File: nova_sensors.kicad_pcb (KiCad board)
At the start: 2 copper layers, 100 x 100 mm, 83 parts, among them J1 Conn_01x02_Socket, J10 Conn_01x03_Socket, J11 Conn_01x03_Socket, J12 Conn_01x03_Socket, J13 Conn_01x03_Socket, J4 Conn_01x04_Socket, J5 Conn_01x02_Socket, J6 Conn_01x02_Socket, J7 Conn_01x02_Socket, J8 Conn_01x02_Socket, J9 Conn_01x02_Socket, SW1 SW_Push, SW2 SW_DIP_x02, SW3 SW_DIP_x02, U1 AT32F455CET7, U2 MAX3232, U3 MAX13487EESA+T, U4 MAX13487EESA+T, U5 LD1117S33TR, U6 XL1509-ADJ, Y1 8Mhz, Y2 32768hz

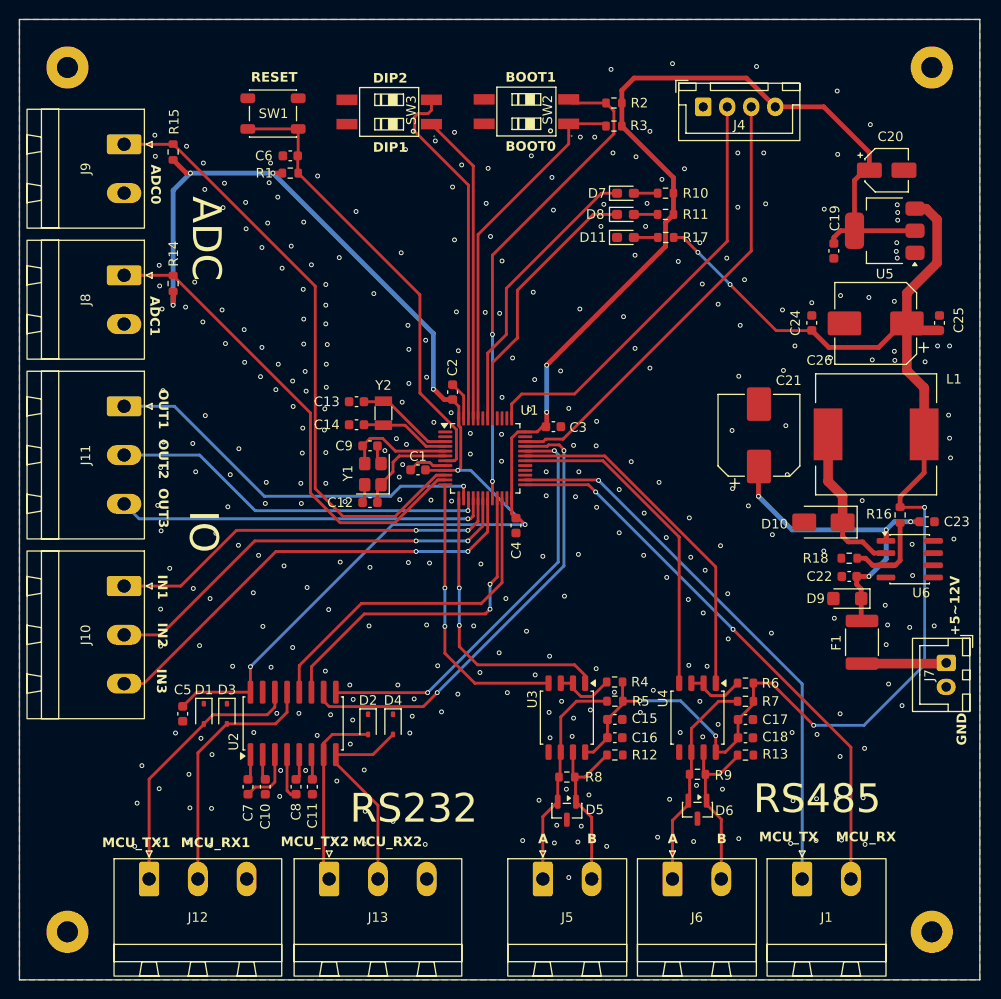
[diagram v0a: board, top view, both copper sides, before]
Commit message: refact: 重新排列引脚，使得布局更合理，同时压缩板子面积
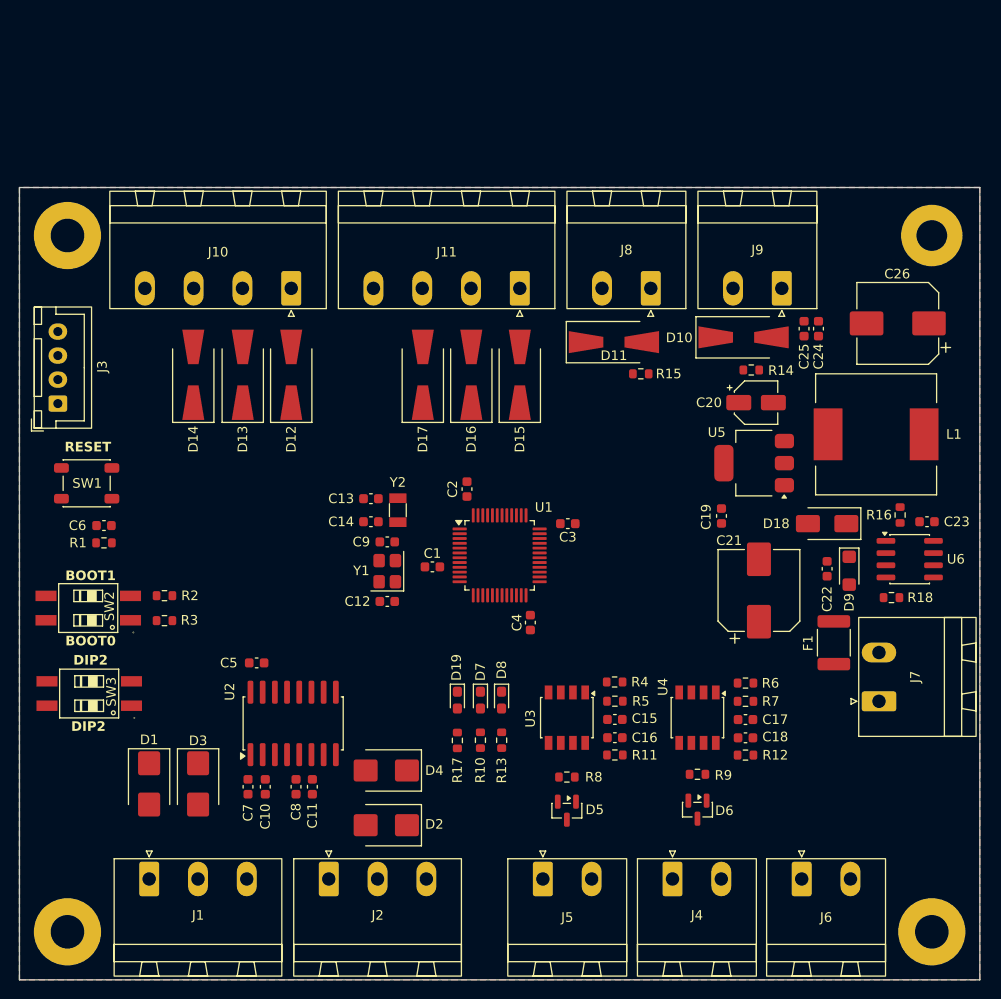
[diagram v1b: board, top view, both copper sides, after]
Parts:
- removed J12, J13: Conn_01x03_Socket, Connector_Phoenix_MSTB:PhoenixContact_MSTBA_2,5_3-G-5,08_1x03_P5.08mm_Horizontal
- added D12: SMAJ3.3CA, Diode_SMD:D_SMA-SMB_Universal_Handsoldering, F.Cu at (28.3, 147.0)
- added D13: SMAJ3.3CA, Diode_SMD:D_SMA-SMB_Universal_Handsoldering, F.Cu at (23.2, 147.0)
- added D14: SMAJ3.3CA, Diode_SMD:D_SMA-SMB_Universal_Handsoldering, F.Cu at (18.1, 147.0)
- added D15: SMAJ3.3CA, Diode_SMD:D_SMA-SMB_Universal_Handsoldering, F.Cu at (52.1, 147.0)
- added D16: SMAJ3.3CA, Diode_SMD:D_SMA-SMB_Universal_Handsoldering, F.Cu at (47.0, 147.0)
- added D17: SMAJ3.3CA, Diode_SMD:D_SMA-SMB_Universal_Handsoldering, F.Cu at (42.0, 147.0)
- added D18: SS34, Diode_SMD:D_SMA, F.Cu at (84.1, 162.5)
- added D19: GREEN, LED_SMD:LED_0603_1608Metric_Pad1.05x0.95mm_HandSolder, F.Cu at (45.6, 180.9)
- added J2: Conn_01x03_Socket, Connector_Phoenix_MSTB:PhoenixContact_MSTBA_2,5_3-G-5,08_1x03_P5.08mm_Horizontal, F.Cu at (32.2, 199.5)
- added J3: Conn_01x04_Socket, Connector_JST:JST_XH_B4B-XH-A_1x04_P2.50mm_Vertical, F.Cu at (4.00, 150.0)
- C24: value 100nF/35V -> 100nF/16V
- C25: value 22uF/35V -> 22uF/16V
- C26: value 220uF/35V -> 220uF/16V
- D1, D2, D3, D4: value SGSD15C -> SMAJ8.0CA; footprint Diode_SMD:D_SOD-323 -> Diode_SMD:D_SMB
- D10: value SS34 -> SMAJ3.3CA; footprint Diode_SMD:D_SMA -> Diode_SMD:D_SMA-SMB_Universal_Handsoldering
- D11: value GREEN -> SMAJ3.3CA; footprint LED_SMD:LED_0603_1608Metric_Pad1.05x0.95mm_HandSolder -> Diode_SMD:D_SMA-SMB_Universal_Handsoldering
- H1: footprint MountingHole:MountingHole_2.2mm_M2_Pad -> MountingHole:MountingHole_3.2mm_M3_Pad
- H2, H3, H4: footprint MountingHole:MountingHole_2.2mm_M2_Pad -> MountingHole:MountingHole_3.5mm_Pad
- J1: value Conn_01x02_Socket -> Conn_01x03_Socket; footprint Connector_Phoenix_MSTB:PhoenixContact_MSTBA_2,5_2-G-5,08_1x02_P5.08mm_Horizontal -> Connector_Phoenix_MSTB:PhoenixContact_MSTBA_2,5_3-G-5,08_1x03_P5.08mm_Horizontal
- J10, J11: value Conn_01x03_Socket -> Conn_01x04_Socket; footprint Connector_Phoenix_MSTB:PhoenixContact_MSTBA_2,5_3-G-5,08_1x03_P5.08mm_Horizontal -> Connector_Phoenix_MSTB:PhoenixContact_MSTBA_2,5_4-G-5,08_1x04_P5.08mm_Horizontal
- J4: value Conn_01x04_Socket -> Conn_01x02_Socket; footprint Connector_JST:JST_XH_B4B-XH-A_1x04_P2.50mm_Vertical -> Connector_Phoenix_MSTB:PhoenixContact_MSTBA_2,5_2-G-5,08_1x02_P5.08mm_Horizontal
- J7: footprint Connector_JST:JST_XH_B2B-XH-A_1x02_P2.50mm_Vertical -> Connector_Phoenix_MSTB:PhoenixContact_MSTBA_2,5_2-G-5,08_1x02_P5.08mm_Horizontal
- R11: value 1K -> 360R
- R13: value 360R -> 1K
- U3, U4: footprint Package_SO:SOIC-8_5.3x5.3mm_P1.27mm -> Package_SO:SSOP-8_3.95x5.21x3.27mm_P1.27mm
- moved J4 80.5 mm to (68.0, 199.5)
- moved J9 70.1 mm to (79.4, 138.0), turned to 180 degrees
- moved R3 69.6 mm to (15.1, 172.6)
- moved R2 69.4 mm to (15.1, 170.0)
- moved SW2 69.0 mm to (7.17, 171.3)
- moved SW3 68.1 mm to (7.28, 180.2)
- moved J1 68.0 mm to (13.5, 199.5)
- moved R14 60.9 mm to (76.2, 146.5), turned to 0 degrees
- moved R10 60.1 mm to (48.0, 185.1), turned to 90 degrees
- moved R17 56.7 mm to (45.6, 185.1), turned to 90 degrees
- moved R11 56.5 mm to (62.0, 186.6), turned to 0 degrees
- moved D7 54.9 mm to (48.0, 180.9), turned to -90 degrees
- moved J8 54.9 mm to (65.7, 138.0), turned to 180 degrees
- moved R15 53.9 mm to (64.7, 146.9), turned to 0 degrees
- moved D8 52.2 mm to (50.2, 180.9), turned to -90 degrees
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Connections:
- D10 pad 1: Net-(D10-K) -> GND
- D10 pad 2: GND -> /ADC_IN1
- D11 pad 2: Net-(D11-A) -> /ADC_IN0
- D7 pad 1: /~{LED_STA_ERR} -> /~{LED_ERR}
- D8 pad 1: /~{LED_STA_RUN} -> /~{LED_RUN}
- F1 pad 1: Net-(J7-Pin_1) -> Net-(J7-Pin_2)
- J1 pad 1: /TTL_TX -> Net-(D1-A2)
- J1 pad 2: /TTL_RX -> Net-(D3-A2)
- J10 pad 1: /IN1 -> /IN3
- J10 pad 3: /IN3 -> /IN1
- J11 pad 1: /OUT1 -> /OUT3
- J11 pad 3: /OUT3 -> /OUT1
- J4 pad 1: GND -> Net-(D6-A2)
- J4 pad 2: /SWCLK -> Net-(D6-A1)
- J6 pad 1: Net-(D6-A2) -> /TTL_TX
- J6 pad 2: Net-(D6-A1) -> /TTL_RX
- J7 pad 1: Net-(J7-Pin_1) -> GND
- J7 pad 2: GND -> Net-(J7-Pin_2)
- J8 pad 1: /ADC_IN1 -> /ADC_IN0
- J9 pad 1: /ADC_IN0 -> /ADC_IN1
- L1 pad 1: Net-(D10-K) -> Net-(D18-K)
- R11 pad 1: +3V3 -> Net-(D5-A1)
- R11 pad 2: Net-(D8-A) -> GND
- R12 pad 1: Net-(D5-A1) -> Net-(D6-A1)
- R13 pad 1: Net-(D6-A1) -> +3V3
- R13 pad 2: GND -> Net-(D8-A)
- R17 pad 2: Net-(D11-A) -> Net-(D19-A)
- SW3 pad 1: /DIP1 -> /DIP2
- SW3 pad 2: /DIP2 -> /DIP1
- U1 pad 10: /ADC_IN0 -> /DIP1
- U1 pad 11: /ADC_IN1 -> /DIP2
- U1 pad 12: /485_2_TX -> /232_1_TX
- U1 pad 13: /485_2_RX -> /232_1_RX
- U1 pad 14: /OUT1 -> /~{LED_ERR}
- U1 pad 15: /OUT2 -> /~{LED_RUN}
- U1 pad 16: /OUT3 -> unconnected-(U1-PA6-Pad16)
- U1 pad 17: /IN1 -> unconnected-(U1-PA7-Pad17)
- U1 pad 18: /IN2 -> /ADC_IN0
- U1 pad 19: /IN3 -> /ADC_IN1
- U1 pad 21: /232_1_TX -> /232_2_TX
- U1 pad 22: /232_1_RX -> /232_2_RX
- U1 pad 25: /TTL_RX -> /485_1_RX
- U1 pad 26: /TTL_TX -> /485_1_TX
- U1 pad 30: /485_1_TX -> /485_2_TX
- U1 pad 31: /485_1_RX -> /485_2_RX
- U1 pad 32: /232_2_RX -> /TTL_RX
- U1 pad 33: /232_2_TX -> /TTL_TX
- U1 pad 40: unconnected-(U1-PB4-Pad40) -> /OUT3
- U1 pad 41: /~{LED_STA_RUN} -> /OUT2
- U1 pad 42: /~{LED_STA_ERR} -> /OUT1
- U1 pad 43: unconnected-(U1-PB7-Pad43) -> /IN3
- U1 pad 45: /DIP1 -> /IN2
- U1 pad 46: /DIP2 -> /IN1
- U3 pad 1: /485_2_RX -> /485_1_RX
- U3 pad 4: /485_2_TX -> /485_1_TX
- U4 pad 1: /485_1_RX -> /485_2_RX
- U4 pad 4: /485_1_TX -> /485_2_TX
- U6 pad 2: Net-(D10-K) -> Net-(D18-K)
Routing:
- net +3V3: track 229.9 -> 0.00 mm, vias 9 -> 0
- net +5V: track 142.5 -> 0.00 mm, vias 6 -> 0
- net /ADC_IN0: track 63.6 -> 0.00 mm
- net /TTL_RX: track 59.0 -> 0.00 mm, vias 2 -> 0
- net /TTL_TX: track 57.9 -> 0.00 mm, vias 1 -> 0
- net /ADC_IN1: track 50.8 -> 0.00 mm
- net /BOOT1: track 50.8 -> 0.00 mm, vias 2 -> 0
- net /232_2_TX: track 48.7 -> 0.00 mm, vias 2 -> 0
- net /IN3: track 47.9 -> 0.00 mm, vias 2 -> 0
- net /~{RST}: track 47.7 -> 0.00 mm
- net /SWDIO: track 46.8 -> 0.00 mm
- net /SWCLK: track 45.0 -> 0.00 mm
- net /IN2: track 44.9 -> 0.00 mm, vias 2 -> 0
- net /232_2_RX: track 43.6 -> 0.00 mm, vias 2 -> 0
- net /IN1: track 42.0 -> 0.00 mm, vias 2 -> 0
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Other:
- board size 100 x 100 mm -> 100 x 82.5 mm
- board text removed: "+5~12V"
- board text removed: "A"
- board text removed: "ADC"
- board text removed: "ADC0"
- board text removed: "ADC1"
- board text removed: "B"
- board text removed: "DIP1"
- board text removed: "GND"
- board text removed: "IN1"
- board text removed: "IN2"
- board text removed: "IN3"
- board text removed: "IO"
- board text removed: "MCU_RX"
- board text removed: "MCU_RX1"
- board text removed: "MCU_RX2"
- board text removed: "MCU_TX"
- board text removed: "MCU_TX1"
- board text removed: "MCU_TX2"
- board text removed: "OUT1"
- board text removed: "OUT2"
- board text removed: "OUT3"
- board text removed: "RS232"
- board text removed: "RS485"

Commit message: refact: 完成V0.0.2版本的布线和DRC检测
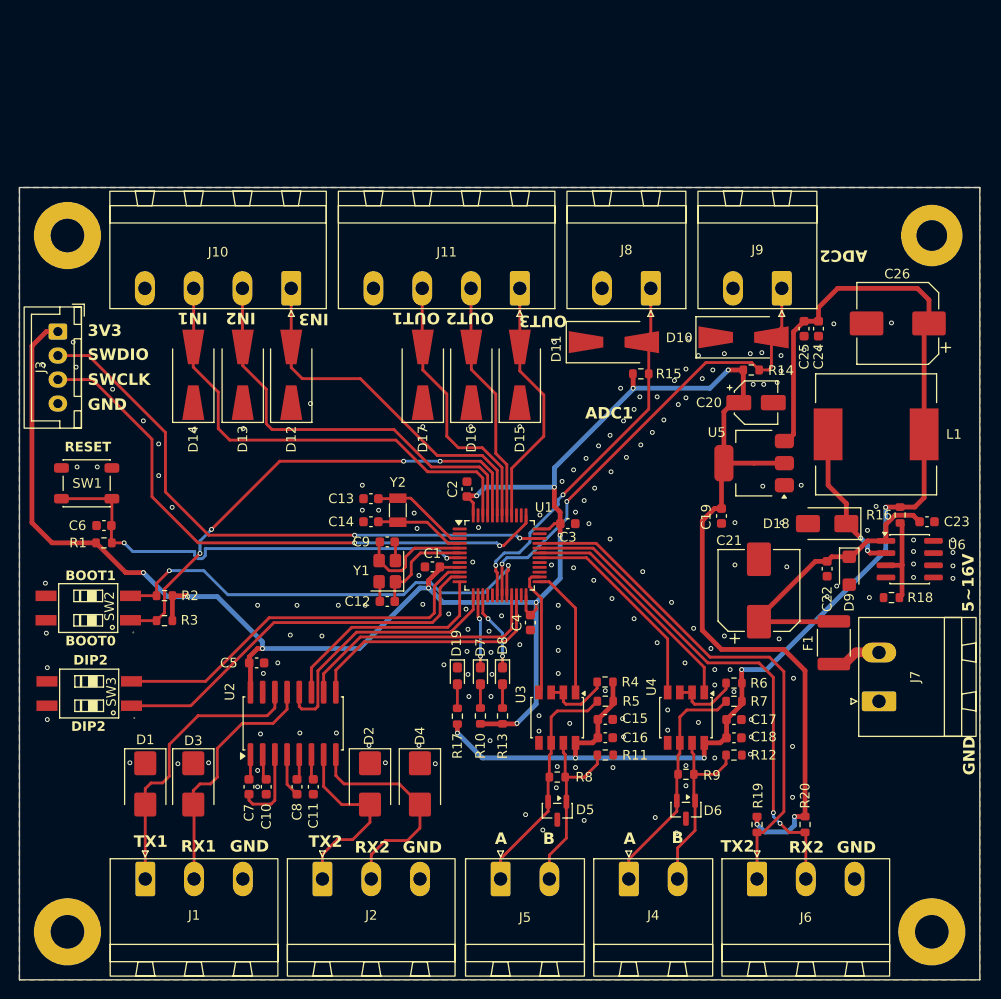
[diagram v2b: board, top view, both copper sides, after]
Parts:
- added R19: 4K7, Resistor_SMD:R_0603_1608Metric, F.Cu at (76.8, 193.8)
- added R20: 4K7, Resistor_SMD:R_0603_1608Metric, F.Cu at (81.8, 193.8)
- C25: value 22uF/16V -> 22uF/10V
- D1, D2, D3, D4: value SMAJ8.0CA -> SMAJ5.0CA
- J6: value Conn_01x02_Socket -> Conn_01x03_Socket; footprint Connector_Phoenix_MSTB:PhoenixContact_MSTBA_2,5_2-G-5,08_1x02_P5.08mm_Horizontal -> Connector_Phoenix_MSTB:PhoenixContact_MSTBA_2,5_3-G-5,08_1x03_P5.08mm_Horizontal
- U3, U4: value MAX13487EESA+T -> MAX13488EESA+T
- moved J3 7.50 mm to (4.00, 142.5), turned to -90 degrees
- moved J6 4.65 mm to (76.8, 199.5)
- moved D2 4.62 mm to (36.5, 189.6), turned to -90 degrees
- moved J4 4.55 mm to (63.5, 199.5)
- moved J5 4.40 mm to (50.1, 199.5)
- moved D4 3.77 mm to (41.7, 189.6), turned to -90 degrees
- moved D8 2.53 mm to (50.3, 178.3)
- moved R13 2.53 mm to (50.3, 182.5)
- moved D19 2.53 mm to (45.6, 178.3)
- moved D7 2.53 mm to (48.0, 178.3)
- moved R10 2.53 mm to (48.0, 182.5)
- moved R17 2.52 mm to (45.6, 182.6)
- moved C17 1.20 mm to (74.4, 182.9)
- moved C18 1.20 mm to (74.4, 184.8)
- moved D6 1.20 mm to (69.4, 192.3)
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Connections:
- J3 pad 1: GND -> +3V3
- J3 pad 2: /SWCLK -> /SWDIO
- J3 pad 3: /SWDIO -> /SWCLK
- J3 pad 4: +3V3 -> GND
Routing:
- net +3V3: track 0.00 -> 244.6 mm, vias 0 -> 13
- net +5V: track 0.00 -> 129.3 mm, vias 0 -> 5
- net /SWDIO: track 0.00 -> 61.7 mm, vias 0 -> 2
- net /SWCLK: track 0.00 -> 61.2 mm, vias 0 -> 2
- net /TTL_TX: track 0.00 -> 54.1 mm
- net /TTL_RX: track 0.00 -> 53.3 mm, vias 0 -> 2
- net /BOOT0: track 0.00 -> 51.7 mm, vias 0 -> 4
- net /ADC_IN1: track 0.00 -> 50.0 mm, vias 0 -> 2
- net /IN1: track 0.00 -> 49.3 mm
- net /~{RST}: track 0.00 -> 48.3 mm, vias 0 -> 2
- net /BOOT1: track 0.00 -> 47.7 mm, vias 0 -> 2
- net /IN2: track 0.00 -> 44.6 mm
- net /DIP2: track 0.00 -> 41.4 mm
- net /DIP1: track 0.00 -> 40.5 mm
- net /ADC_IN0: track 0.00 -> 40.2 mm, vias 0 -> 2
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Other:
- board text added: "3V3"
- board text added: "5~16V"
- board text added: "A"
- board text added: "ADC1"
- board text added: "ADC2"
- board text added: "B"
- board text added: "GND"
- board text added: "IN1"
- board text added: "IN2"
- board text added: "IN3"
- board text added: "OUT1"
- board text added: "OUT2"
- board text added: "OUT3"
- board text added: "RX1"
- board text added: "RX2"
- board text added: "SWCLK"
- board text added: "SWDIO"
- board text added: "TX1"
- board text added: "TX2"

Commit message: refact: 调整PCB丝印和原理图符号位置
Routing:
- net GND: vias 172 -> 173
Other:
- board text added: "RS232"
- board text added: "RS485"
- board text added: "RX"
- board text added: "TTL"
- board text added: "TX"

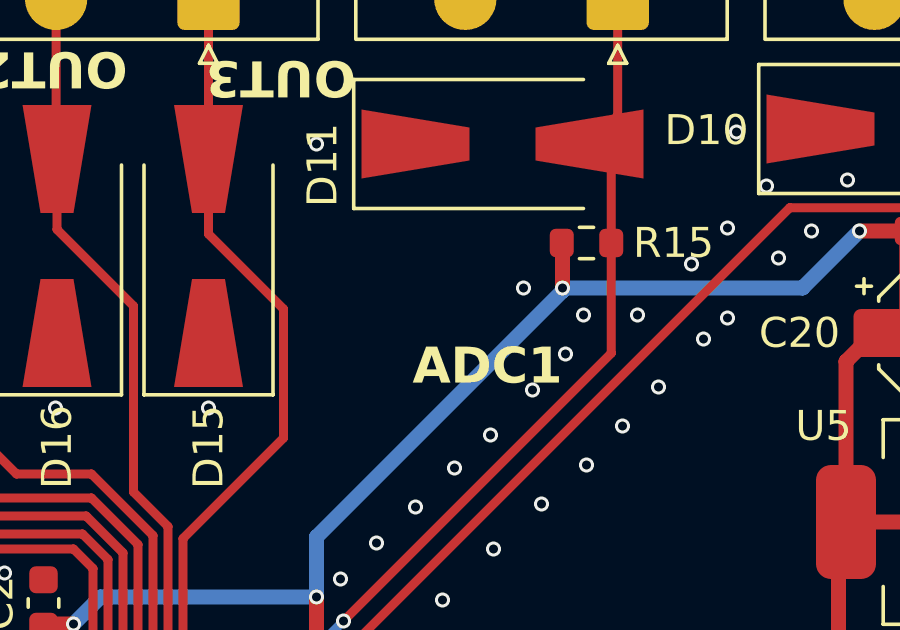
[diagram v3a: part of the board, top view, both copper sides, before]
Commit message: refact: 调整丝印与网络标签，更新AT32 WorkBench配置
- PCB: 调整ADC1丝印位置并取消锁定
- SCH: 网络标签重命名 ADC_IN0->ADC1, ADC_IN1->ADC2
- ATWP: 工程重命名为nova_sensors，新增WDT/TMR1/DMA及串口中断等外设配置
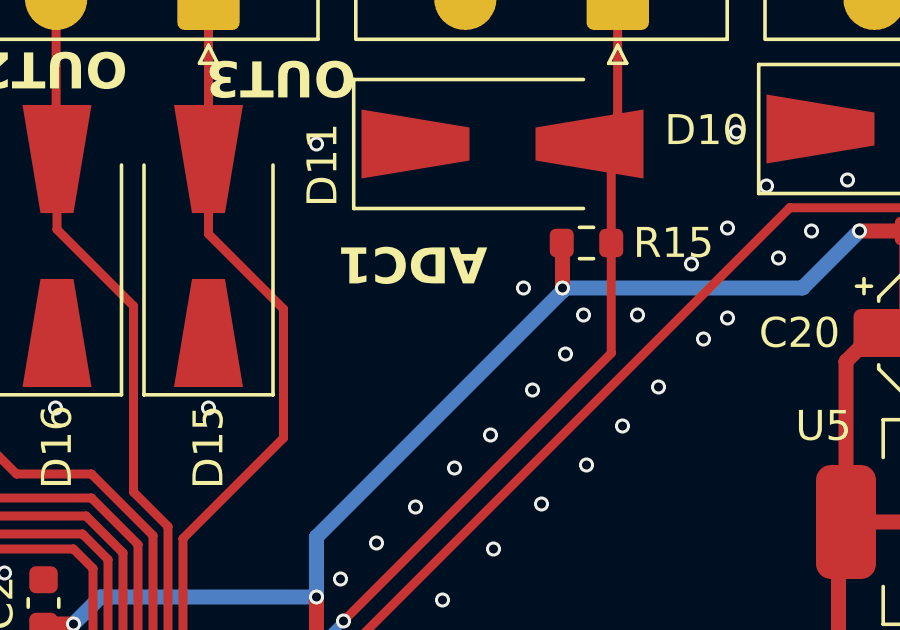
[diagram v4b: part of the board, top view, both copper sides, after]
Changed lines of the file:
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@@
-		)
-	)
-	(gr_text "ADC1"
-		(locked yes)
-		(at 58.9 151.7 0)
-		(layer "F.SilkS")
-		(effects
-			(font
-				(size 1.2 1.2)
-				(thickness 0.2)
-				(bold yes)
-			)
-			(justify left bottom)
 		)
 	)
@@
 		(layer "F.SilkS")
 		(effects
+			(font
+				(size 1.2 1.2)
+				(thickness 0.2)
+				(bold yes)
+			)
+			(justify left bottom)
+		)
+	)
+	(gr_text "ADC1"
+		(at 61.4 146.9 180)
+		(layer "F.SilkS")
+		(effects

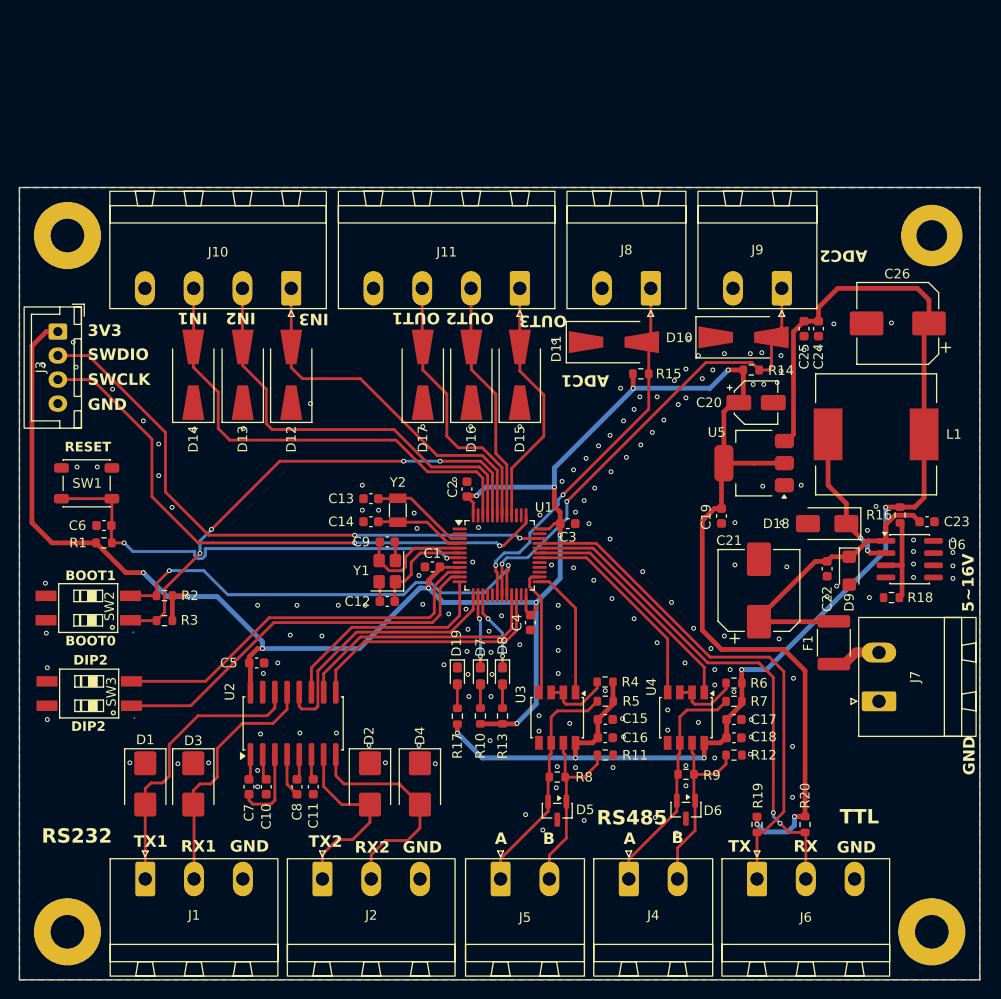
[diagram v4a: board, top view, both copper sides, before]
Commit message: fix: 修复工程专用符号库中485芯片缺失的问题，同时调整了485芯片的封装并更新了pcb
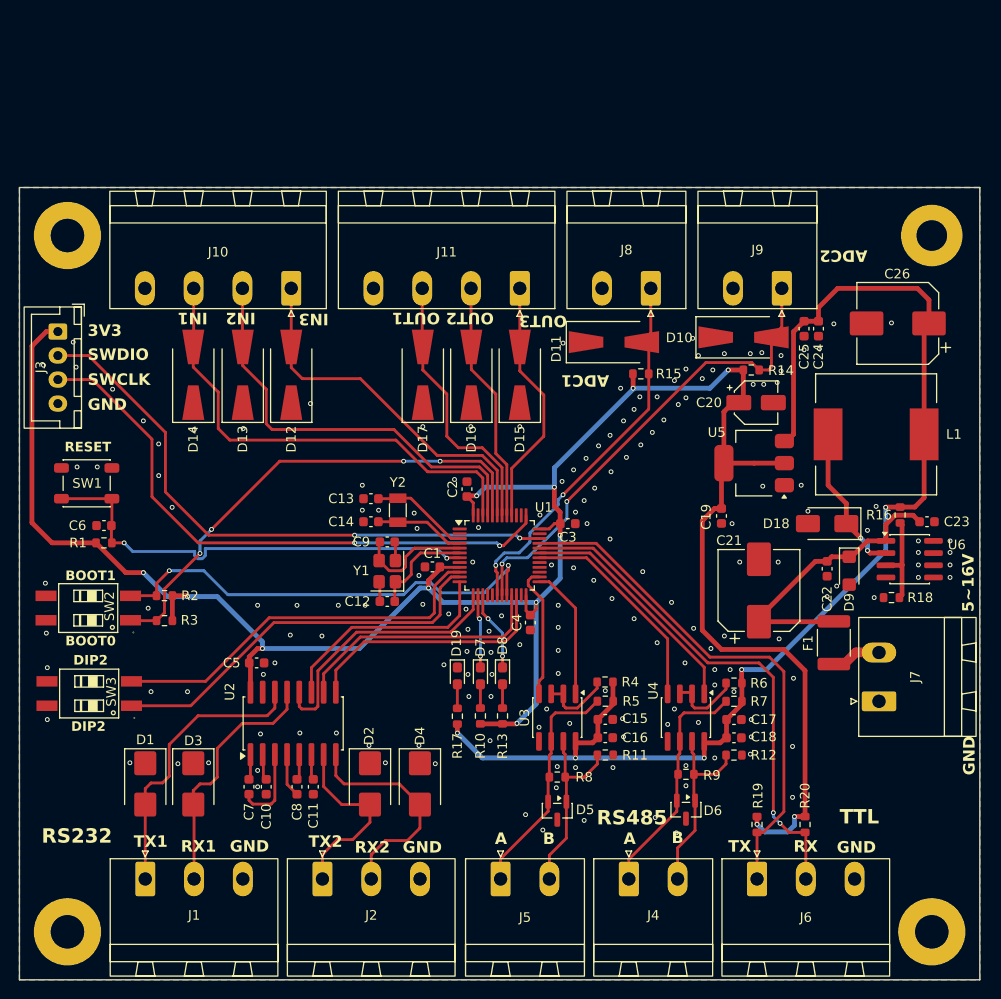
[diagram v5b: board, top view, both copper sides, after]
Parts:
- R17: value 1K -> 4K7
- U3, U4: value MAX13488EESA+T -> MAX13488; footprint Package_SO:SSOP-8_3.95x5.21x3.27mm_P1.27mm -> Package_SO:SOIC-8_3.9x4.9mm_P1.27mm
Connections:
- net /ADC_IN0 renamed /ADC1
- net /ADC_IN1 renamed /ADC2
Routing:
- net Net-(U3-~{RE}): track 7.20 -> 7.77 mm
- net Net-(U4-~{RE}): track 7.16 -> 7.72 mm
- net GND: vias 173 -> 176

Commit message: fix: 调整电源指示灯的限流电阻大小，使其与其他两个灯亮度相近；调整装配图的说明文字位置，使其易于辨认
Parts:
- R17: value 4K7 -> 6K8
